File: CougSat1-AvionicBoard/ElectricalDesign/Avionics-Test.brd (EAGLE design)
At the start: 90.4 x 95.8 mm, 213 parts, among them J1 +X Panel GPS, J10 iFJR SD1, J11 -Y, J12 +Z, J13 +X, J14 -Z, J15 +Y, J16 IFJR SD0, J2 IHU SD1, J3 SWD, J4 CougSat Card, J5 -X, J6 IHU SD0, J8 SWD, J9 SWD, U1 STM32L476RGT, U10 BNO055, U11 M24M01, U12 TXS0102DQM, U13 TXS0102DQM, U14 AD8515, U15 BNO055, U16 BNO055, U17 TXS0102DQM, U18 TXS0102DQM, U19 AD8515, U2 STM32L476RGT, U20 INA199C2, U21 INA199C2, U22 TXS0102DQM, U23 TXS0102DQM, U24 AD8515, U25 AD7291, U26 AD7291, U27 TXS0102DQM, U28 INA199C2, U29 AD8515, U3 STM32L476RGT, U30 DRV8837, U4 M24M01, U5 TXS0102DQM, U6 DRV8837, U7 DRV8837, U8 AD7291, U9 Venus838FLPx-L, Y1 8MHz ±10ppm, Y10 32.768kHz ±10ppm, Y2 32.768kHz ±10ppm, Y3 8MHz ±10ppm, Y4 32.768kHz ±10ppm, Y5 8MHz ±10ppm, Y6 32.768kHz ±10ppm, Y7 32.768kHz ±10ppm, Y8 32.768kHz ±10ppm

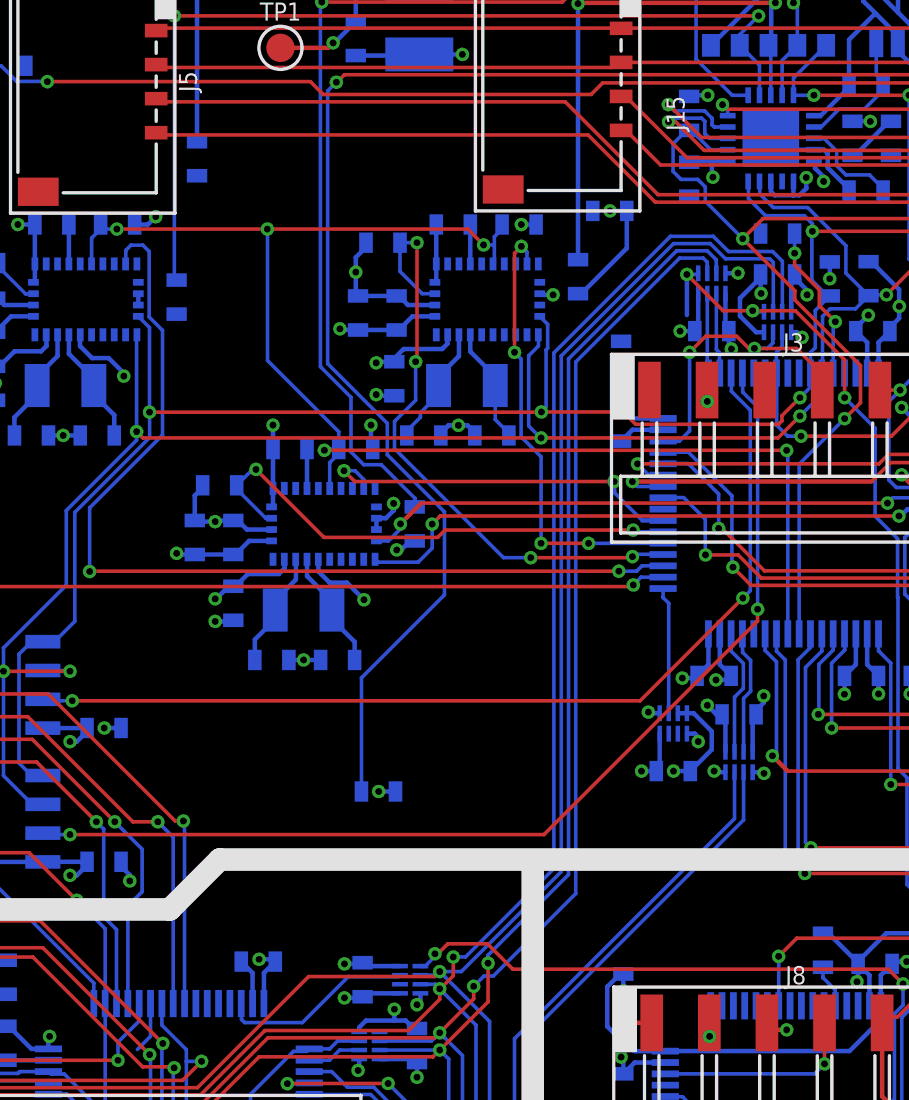
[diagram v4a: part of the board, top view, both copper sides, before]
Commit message: Began Routing DGND
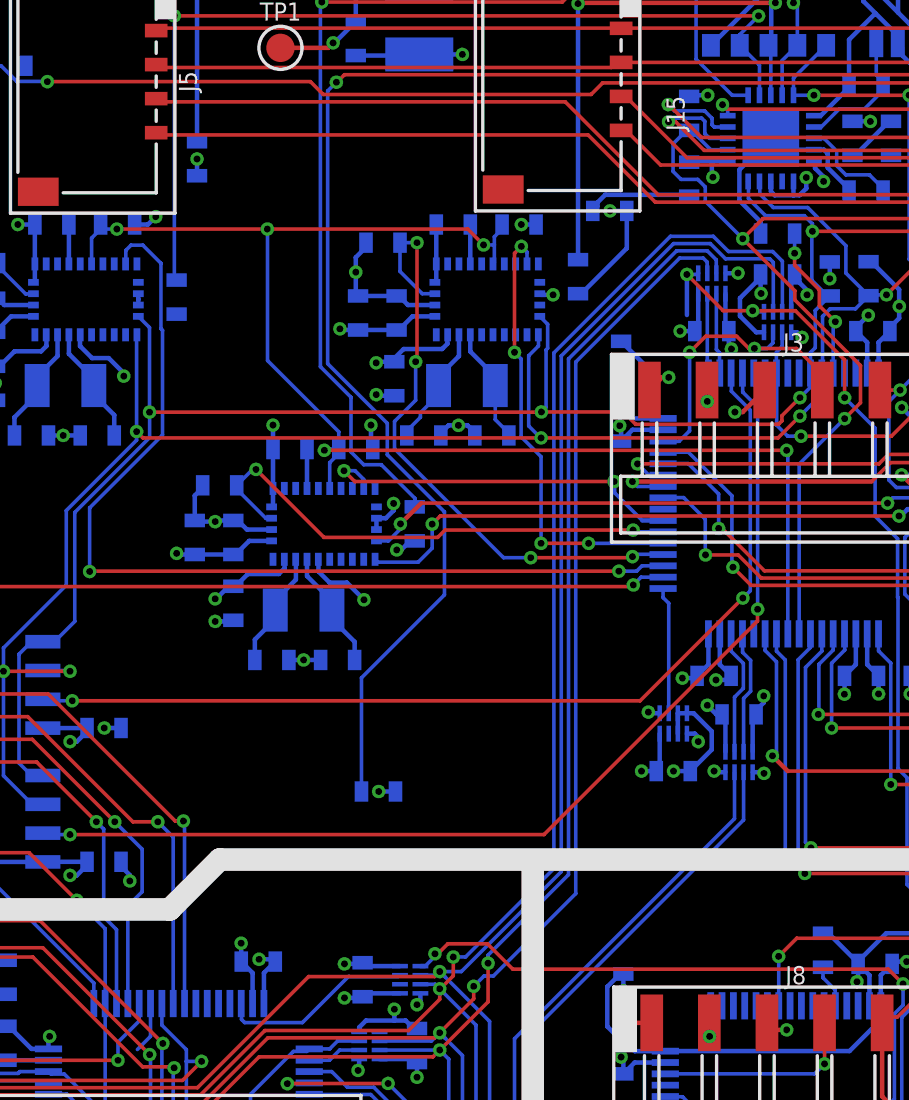
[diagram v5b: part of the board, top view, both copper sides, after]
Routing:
- net DGND: track 576.8 -> 618.8 mm, vias 69 -> 72
- net ADCS_SWD_VSENCE: track 0.00 -> 3.84 mm, vias 0 -> 1
- net PGND: track 77.6 -> 78.3 mm, vias 6 -> 7
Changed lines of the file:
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@@
 <wire x1="79.41" y1="15.79" x2="79.868653125" y2="15.331346875" width="0.2" layer="16"/>
 <wire x1="77.24230625" y1="15.79" x2="79.41" y2="15.79" width="0.2" layer="16"/>
+<wire x1="26.8" y1="33.35" x2="26.8" y2="34.09" width="0.2" layer="16"/>
+<via x="26.8" y="34.09" extent="1-16" drill="0.3"/>
 <wire x1="71.8" y1="14.4" x2="74.6" y2="12.95" width="0" layer="19" extent="16-16"/>
 <wire x1="26.8" y1="33.35" x2="71.8" y2="14.4" width="0" layer="19" extent="16-16"/>
@@
 <wire x1="21.64" y1="25.84230625" x2="22.17230625" y2="25.31" width="0.2" layer="16"/>
 <wire x1="22.17230625" y1="25.31" x2="22.90769375" y2="25.31" width="0.2" layer="16"/>
-<wire x1="24.2125" y1="28.15" x2="24.2125" y2="27.65" width="0.2" layer="16"/>
+<wire x1="24.2125" y1="28.15" x2="24.2125" y2="27.9" width="0.2" layer="16"/>
+<wire x1="24.2125" y1="27.9" x2="24.2125" y2="27.65" width="0.2" layer="16"/>
 <wire x1="25.9" y1="16.7" x2="20.9" y2="21.7" width="0.2" layer="2"/>
 <wire x1="20.9" y1="21.7" x2="20.9" y2="21.9" width="0.2" layer="2"/>
@@
 <wire x1="51.65" y1="28.18" x2="51.67" y2="28.16" width="0.2" layer="16"/>
 <via x="51.67" y="28.16" extent="1-16" drill="0.3"/>
-<wire x1="51.67" y1="28.16" x2="52.630003125" y2="27.2" width="0.2" layer="2"/>
-<wire x1="52.630003125" y1="27.2" x2="56.4" y2="27.2" width="0.2" layer="2"/>
+<wire x1="56.4" y1="27.230003125" x2="56.145003125" y2="27.485" width="0.2" layer="2"/>
+<wire x1="56.145003125" y1="27.485" x2="52.345" y2="27.485" width="0.2" layer="2"/>
+<wire x1="51.67" y1="28.16" x2="52.345" y2="27.485" width="0.2" layer="2"/>
+<wire x1="56.4" y1="27.2" x2="56.4" y2="27.230003125" width="0.2" layer="2"/>
 <wire x1="55.55" y1="32.7" x2="55.55" y2="32.765" width="0.2" layer="16"/>
 <wire x1="55.55" y1="32.765" x2="54.61" y2="33.705" width="0.2" layer="16"/>
@@
 <wire x1="54.44269375" y1="34.5" x2="54" y2="34.5" width="0.2" layer="16"/>
 <wire x1="54.61" y1="33.705" x2="54.61" y2="34.33269375" width="0.2" layer="16"/>
+<wire x1="22.71" y1="9" x2="23.835" y2="7.875" width="0.2" layer="2"/>
+<wire x1="23.835" y1="7.875" x2="23.835" y2="2.255" width="0.2" layer="2"/>
+<wire x1="23.835" y1="2.255" x2="26" y2="2.255" width="0.2" layer="2"/>
+<wire x1="26" y1="2.255" x2="28.745" y2="-0.49" width="0.2" layer="2"/>
+<via x="28.745" y="-0.49" extent="1-16" drill="0.3"/>
+<wire x1="28.745" y1="-0.49" x2="28.75" y2="-0.495" width="0.2" layer="16"/>
+<wire x1="28.75" y1="-0.495" x2="28.75" y2="-1.3" width="0.2" layer="16"/>
+<wire x1="51.65" y1="30.8" x2="51.65" y2="31.32146875" width="0.2" layer="16"/>
+<wire x1="51.65" y1="31.32146875" x2="50.715" y2="32.25646875" width="0.2" layer="16"/>
+<wire x1="50.715" y1="32.25646875" x2="50.715" y2="33.615" width="0.2" layer="16"/>
+<wire x1="50.715" y1="33.615" x2="52.1" y2="35" width="0.2" layer="16"/>
+<wire x1="44.45" y1="32.1619625" x2="44.45" y2="32" width="0.2" layer="16"/>
+<wire x1="44.45" y1="32" x2="44.25" y2="31.8" width="0.2" layer="16"/>
+<wire x1="44.45" y1="32.1619625" x2="44.7980375" y2="32.51" width="0.2" layer="16"/>
+<wire x1="48.44" y1="32.51" x2="48.5" y2="32.45" width="0.2" layer="16"/>
+<wire x1="44.7980375" y1="32.51" x2="48.44" y2="32.51" width="0.2" layer="16"/>
+<wire x1="48.1" y1="26.5" x2="49.76" y2="28.16" width="0.2" layer="2"/>
+<wire x1="49.76" y1="28.16" x2="51.67" y2="28.16" width="0.2" layer="2"/>
+<via x="45.438625" y="22.33" extent="1-16" drill="0.3"/>
+<wire x1="48.1" y1="26.5" x2="46.06" y2="24.46" width="0.2" layer="2"/>
+<wire x1="45.438625" y1="23.0466625" x2="45.438625" y2="22.33" width="0.2" layer="2"/>
+<wire x1="46.06" y1="24.46" x2="46.06" y2="23.6680375" width="0.2" layer="2"/>
+<wire x1="46.06" y1="23.6680375" x2="45.438625" y2="23.0466625" width="0.2" layer="2"/>
+<wire x1="45.5" y1="21.65" x2="45.5" y2="22.268625" width="0.2" layer="16"/>
+<wire x1="45.5" y1="22.268625" x2="45.438625" y2="22.33" width="0.2" layer="16"/>
+<via x="50.51690625" y="22.93" extent="1-16" drill="0.3"/>
+<wire x1="49.5319625" y1="22.84" x2="49.6219625" y2="22.93" width="0.2" layer="2"/>
+<wire x1="49.6219625" y1="22.93" x2="50.51690625" y2="22.93" width="0.2" layer="2"/>
+<wire x1="45.438625" y1="22.33" x2="45.948625" y2="22.84" width="0.2" layer="2"/>
+<wire x1="45.948625" y1="22.84" x2="49.5319625" y2="22.84" width="0.2" layer="2"/>
+<wire x1="51.83" y1="23.9" x2="50.86" y2="22.93" width="0.2" layer="1"/>
+<wire x1="50.86" y1="22.93" x2="50.51690625" y2="22.93" width="0.2" layer="1"/>
+<wire x1="48" y1="9.65" x2="48" y2="8.75" width="0.2" layer="16"/>
 <wire x1="72.65" y1="32.8" x2="81.95" y2="41" width="0" layer="19" extent="16-16"/>
 <wire x1="71.1" y1="34.6" x2="72.65" y2="32.8" width="0" layer="19" extent="16-16"/>
 <wire x1="66.35" y1="26.1" x2="65.6" y2="32.45" width="0" layer="19" extent="16-16"/>
-<wire x1="48" y1="8.75" x2="48" y2="9.65" width="0" layer="19" extent="16-16"/>
 <wire x1="51.65" y1="30.8" x2="51.65" y2="29" width="0" layer="19" extent="16-16"/>
-<wire x1="51.83" y1="23.9" x2="51.8" y2="26.45" width="0" layer="19" extent="1-16"/>
-<wire x1="48.9" y1="28.15" x2="51.67" y2="28.16" width="0" layer="19" extent="16-16"/>
 <wire x1="48.5" y1="32.45" x2="51.65" y2="30.8" width="0" layer="19" extent="16-16"/>
-<wire x1="52.1" y1="35" x2="51.65" y2="30.8" width="0" layer="19" extent="16-16"/>
-<wire x1="44.25" y1="31.8" x2="48.5" y2="32.45" width="0" layer="19" extent="16-16"/>
-<wire x1="47.35" y1="22.15" x2="48.1" y2="26.5" width="0" layer="19" extent="16-16"/>
 <wire x1="57.89" y1="-10.4" x2="56.45" y2="-14.75" width="0" layer="19" extent="16-16"/>
 <wire x1="63.3" y1="-10.15" x2="58.95" y2="-10.75" width="0" layer="19" extent="16-16"/>
@@
 <wire x1="35.5" y1="23.65" x2="35.6" y2="26.55" width="0" layer="19" extent="16-16"/>
 <wire x1="37.55" y1="21.9" x2="35.5" y2="23.65" width="0" layer="19" extent="16-16"/>
-<wire x1="24.2125" y1="27.65" x2="21.65" y2="26.3375" width="0" layer="19" extent="16-16"/>
+<wire x1="24.2125" y1="28.15" x2="21.65" y2="26.3375" width="0" layer="19" extent="16-16"/>
 <wire x1="23.45" y1="9" x2="27.6" y2="13.7" width="0" layer="19" extent="16-16"/>
-<wire x1="23.45" y1="3.1" x2="23.45" y2="9" width="0" layer="19" extent="16-16"/>
-<wire x1="28.75" y1="-1.3" x2="23.835" y2="2.255" width="0" layer="19" extent="16-16"/>
 <wire x1="33.3" y1="-1.4" x2="29.25" y2="-3.15" width="0" layer="19" extent="16-16"/>
 <wire x1="35.5" y1="-3.4" x2="35.75" y2="-1.5" width="0" layer="19" extent="16-16"/>
@@
 <contactref element="J3" pad="1"/>
 <contactref element="R36" pad="1"/>
-<wire x1="45.5" y1="26.05" x2="46.75" y2="23.9" width="0" layer="19" extent="1-16"/>
+<wire x1="45.5" y1="26.05" x2="47.09" y2="24.46" width="0.2" layer="16"/>
+<wire x1="47.09" y1="24.46" x2="47.6" y2="24.46" width="0.2" layer="16"/>
+<via x="47.6" y="24.46" extent="1-16" drill="0.3"/>
+<wire x1="47.6" y1="24.46" x2="47.31" y2="24.46" width="0.2" layer="1"/>
+<wire x1="47.31" y1="24.46" x2="46.75" y2="23.9" width="0.2" layer="1"/>
 </signal>
 <signal name="BUS_JTAG_TCK">
@@
 <wire x1="22.065" y1="18.70759375" x2="25.28" y2="21.92259375" width="0.16" layer="16"/>
 <wire x1="25.28" y1="21.92259375" x2="25.28" y2="26.53505" width="0.16" layer="16"/>
-<wire x1="25.28" y1="26.53505" x2="24.69" y2="27.12505" width="0.16" layer="16"/>
-<wire x1="24.69" y1="27.12505" x2="24.69" y2="30.01" width="0.16" layer="16"/>
-<wire x1="24.69" y1="30.01" x2="24.41" y2="30.29" width="0.16" layer="16"/>
+<wire x1="25.28" y1="26.53505" x2="25.21" y2="26.60505" width="0.16" layer="16"/>
+<wire x1="25.21" y1="26.60505" x2="25.21" y2="29.49" width="0.16" layer="16"/>
+<wire x1="25.21" y1="29.49" x2="24.41" y2="30.29" width="0.16" layer="16"/>
 <wire x1="24.41" y1="30.29" x2="23.89" y2="30.29" width="0.16" layer="16"/>
 <wire x1="23.89" y1="30.29" x2="23.66" y2="30.06" width="0.16" layer="16"/>
@@
 <wire x1="75" y1="24.9" x2="80.235" y2="24.9" width="0.2" layer="15"/>
 <wire x1="80.235" y1="24.9" x2="86.035" y2="24.9" width="0.2" layer="15"/>
+<via x="54.425" y="33.0980375" extent="1-16" drill="0.3"/>
+<wire x1="54" y1="34" x2="54.05" y2="33.95" width="0.2" layer="16"/>
+<wire x1="54.05" y1="33.95" x2="54.05" y2="33.68088125" width="0.2" layer="16"/>
+<wire x1="54.05" y1="33.68088125" x2="54.425" y2="33.30588125" width="0.2" layer="16"/>
+<wire x1="54.425" y1="33.30588125" x2="54.425" y2="33.0980375" width="0.2" layer="16"/>
 <wire x1="72.8" y1="34.35" x2="75.85" y2="41.91" width="0" layer="19" extent="16-16"/>
 <wire x1="71.1" y1="34.1" x2="72.8" y2="34.35" width="0" layer="19" extent="16-16"/>
 <wire x1="61.91" y1="34.55" x2="71.1" y2="34.1" width="0" layer="19" extent="16-16"/>
 <wire x1="57.4" y1="35.75" x2="61.91" y2="34.55" width="0" layer="19" extent="16-16"/>
-<wire x1="54.425" y1="33.0980375" x2="55.7" y2="34.25" width="0" layer="19" extent="16-16"/>
+<wire x1="54" y1="34" x2="55.7" y2="34.25" width="0" layer="19" extent="16-16"/>
 <wire x1="58.65" y1="41.81" x2="57.4" y2="35.75" width="0" layer="19" extent="16-16"/>
 <wire x1="75" y1="24.9" x2="72.8" y2="34.35" width="0" layer="19" extent="16-16"/>
 <wire x1="36.6" y1="41.7" x2="54" y2="34" width="0" layer="19" extent="16-16"/>
-<via x="54.425" y="33.0980375" extent="1-16" drill="0.3"/>
-<wire x1="54" y1="34" x2="54.05" y2="33.95" width="0.2" layer="16"/>
-<wire x1="54.05" y1="33.95" x2="54.05" y2="33.68088125" width="0.2" layer="16"/>
-<wire x1="54.05" y1="33.68088125" x2="54.425" y2="33.30588125" width="0.2" layer="16"/>
-<wire x1="54.425" y1="33.30588125" x2="54.425" y2="33.0980375" width="0.2" layer="16"/>
 </signal>
 <signal name="AVDD-1" class="1">

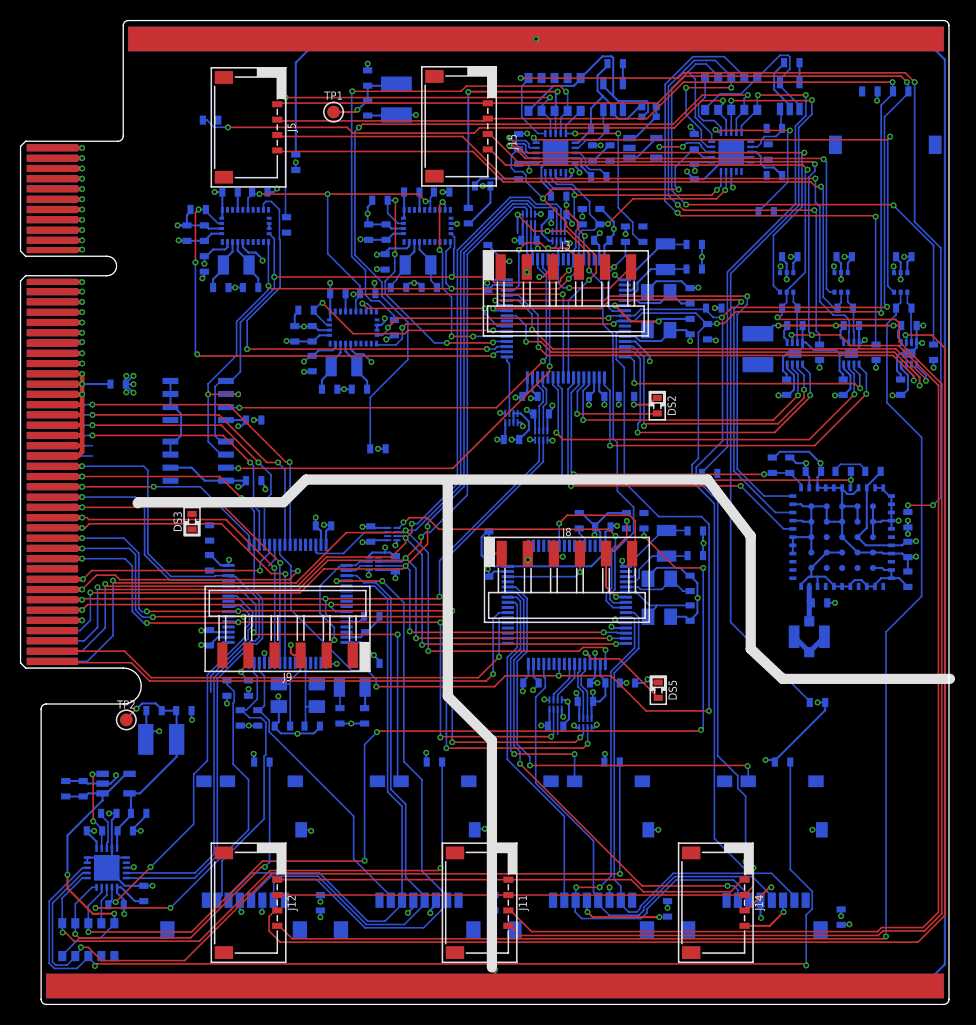
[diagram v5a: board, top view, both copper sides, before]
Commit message: Routed 4 Layer Avionics Board
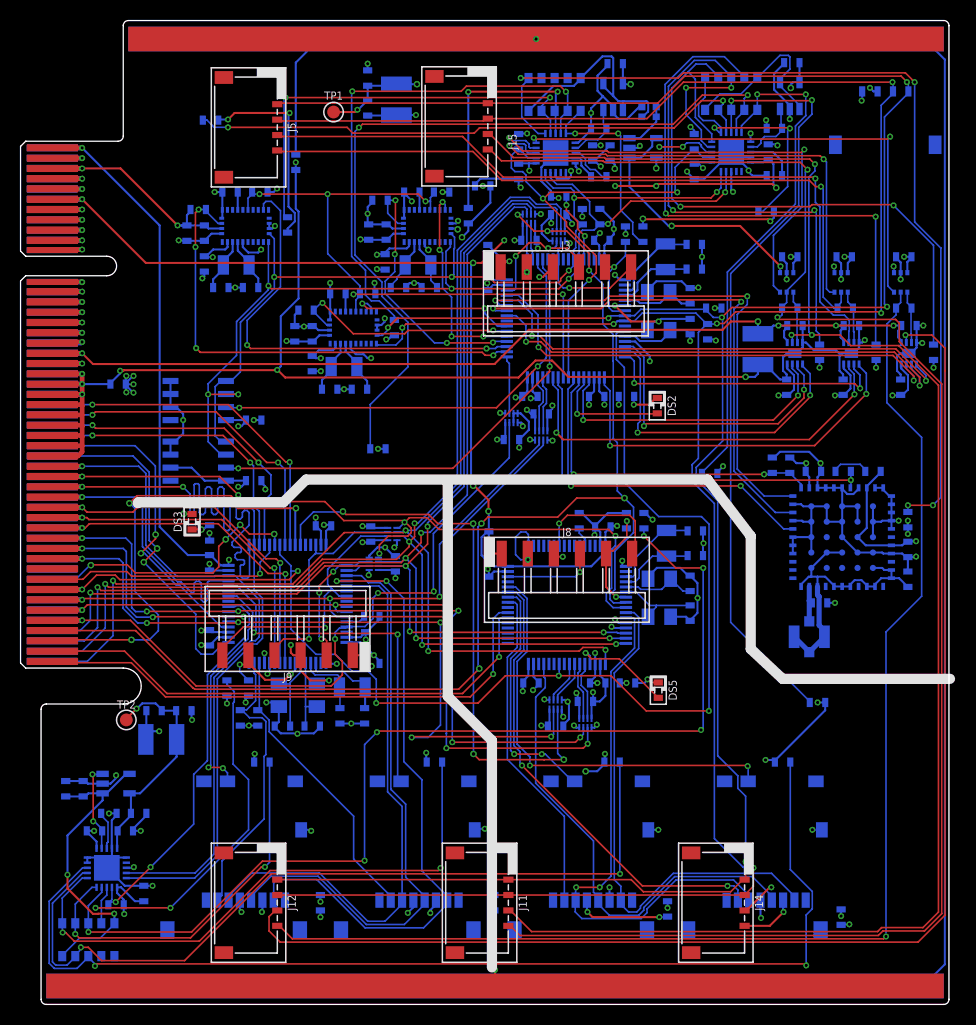
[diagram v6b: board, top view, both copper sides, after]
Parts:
- moved RT16 0.10 mm to (26.0, 28.0)
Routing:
- net DGND: track 618.8 -> 810.5 mm, vias 72 -> 86
- net AGND: track 237.7 -> 415.5 mm, vias 23 -> 38
- net PGND: track 78.3 -> 168.7 mm, vias 7 -> 10
- net 3.3V_0: track 174.5 -> 264.5 mm
- net 3.3V_5: track 132.1 -> 215.7 mm, vias 20 -> 24
- net AVDD-0: track 33.5 -> 116.4 mm, vias 5 -> 13
- net JTAG_EN_ADCS: track 49.5 -> 121.7 mm, vias 3 -> 6
- net VBATT_5: track 27.6 -> 96.5 mm, vias 4 -> 5
- net BUS_I2C0_IRQ: track 5.80 -> 70.6 mm, vias 1 -> 4
- net JTAG_EN_IHU: track 31.4 -> 90.0 mm, vias 2 -> 5
- net BUS_SPI_IFJR_CS: track 2.45 -> 56.4 mm, vias 0 -> 4
- net BUS_I2C1_IRQ: track 24.9 -> 59.7 mm
- net IHU_GPIO-5: track 3.90 -> 34.1 mm, vias 0 -> 2
- net IHU_GPIO-4: track 3.90 -> 31.4 mm, vias 0 -> 2
- net IHU_JTDO: track 0.00 -> 26.7 mm, vias 0 -> 1
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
